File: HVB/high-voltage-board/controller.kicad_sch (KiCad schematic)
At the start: 25 parts, among them J10 Conn_01x05, U4 LD1117S33TR_SOT223, U5 STM32F413CGUx, U6 MCP2551-I-SN, Y1 Crystal

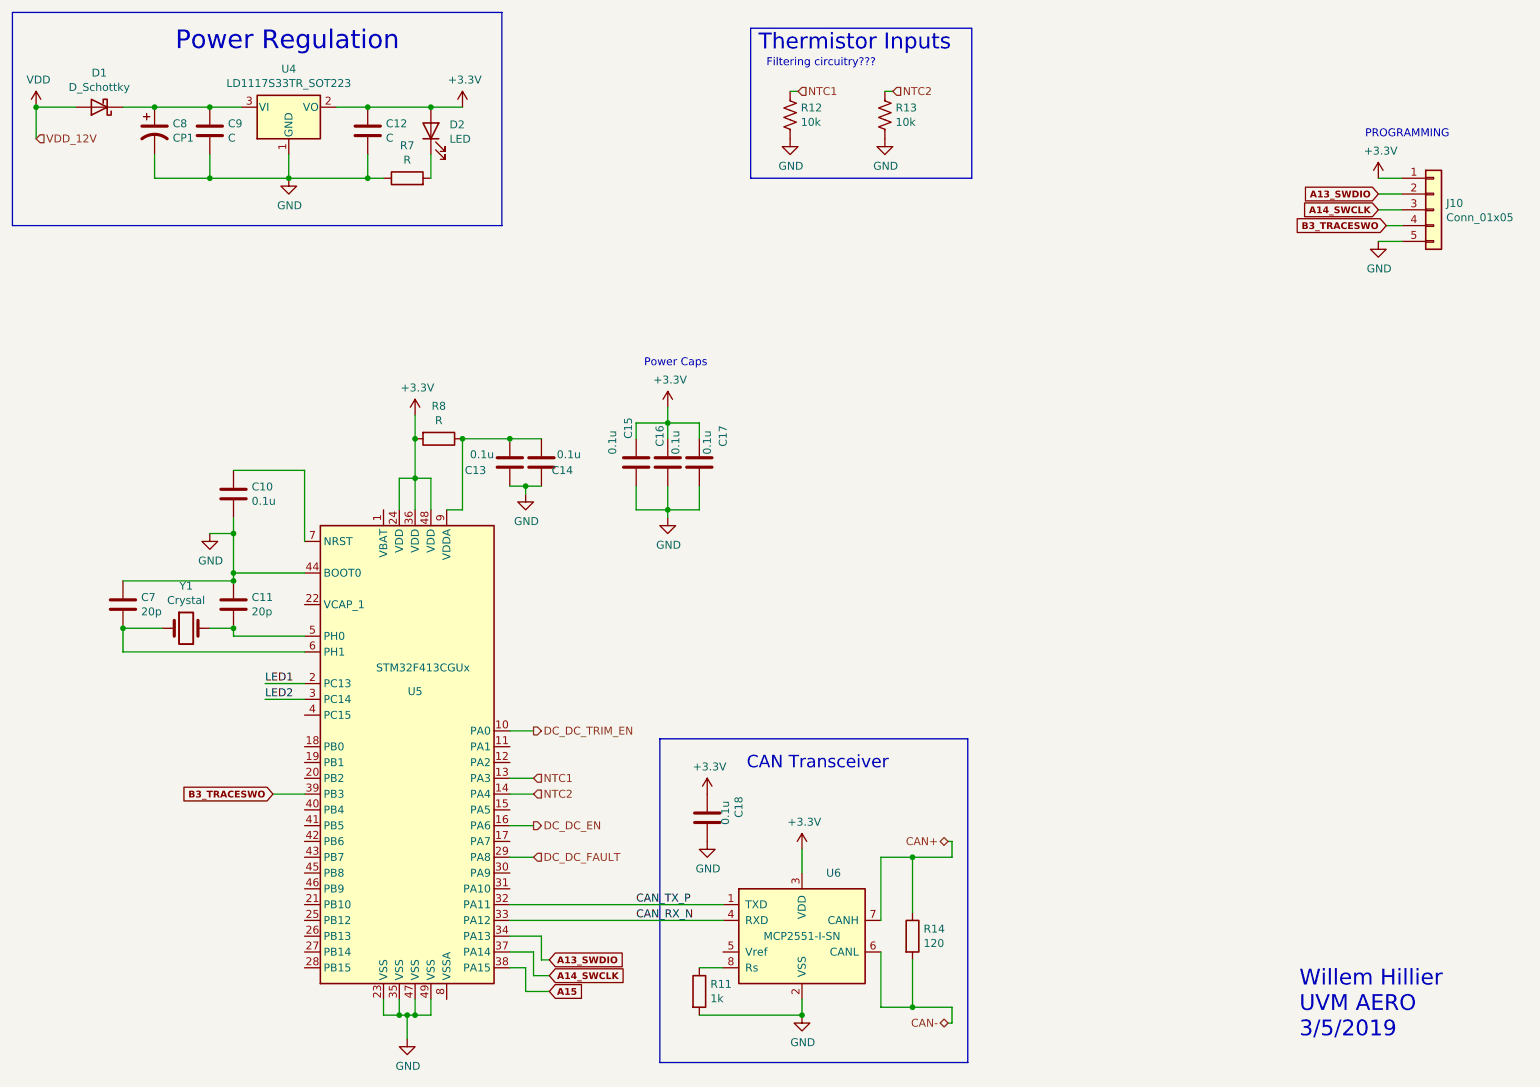
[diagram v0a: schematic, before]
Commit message: working on layout
Updating traces for RCB and organizing HVB
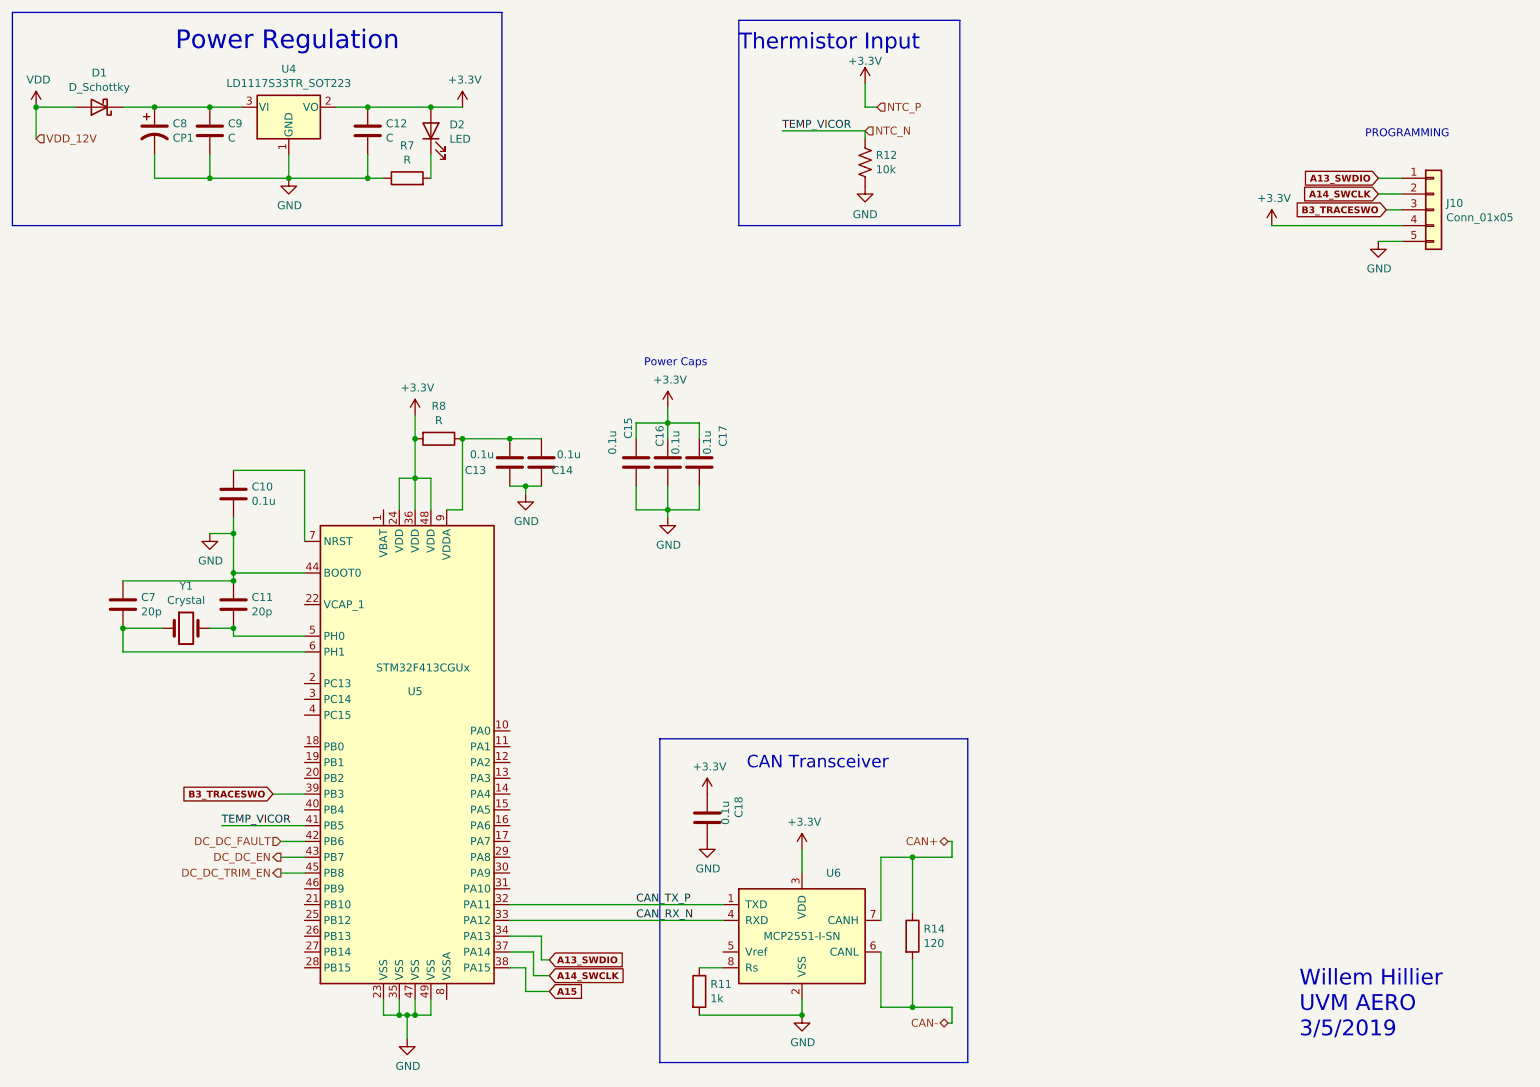
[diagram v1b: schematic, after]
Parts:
- removed R13: 10k, Resistor_SMD:R_0603_1608Metric_Pad0.98x0.95mm_HandSolder, symbol Device:R_US
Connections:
- net +3V3: now also J10.4 (Pin_4); no longer J10.1 (Pin_1)
- net A13_SWDIO: now also J10.1 (Pin_1); no longer J10.2 (Pin_2)
- net A14_SWCLK: now also J10.2 (Pin_2); no longer J10.3 (Pin_3)
- net B3_TRACESWO: now also J10.3 (Pin_3); no longer J10.4 (Pin_4)
- net DC_DC_EN: now also U5.43 (PB7); no longer U5.16 (PA6)
- net DC_DC_FAULT: now also U5.42 (PB6); no longer U5.29 (PA8)
- net DC_DC_TRIM_EN: now also U5.45 (PB8); no longer U5.10 (PA0)
- net NTC_N: now reaches U5.41 (PB5)
- net NTC_N: now also R12.2
- net LED1: no longer names the net of U5.2 (PC13)
- net LED2: no longer names the net of U5.3 (PC14)
- net NTC1: no longer names the net of U5.13 (PA3)
- net NTC1: no longer R12.2
- net NTC2: no longer names the net of U5.14 (PA4)
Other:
- note added: "Thermistor Input"
- note removed: "Filtering circuitry???"
- note removed: "Thermistor Inputs"
- moved on the sheet: R12

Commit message: updating hv layout
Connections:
- net VDD renamed +12V
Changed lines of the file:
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@@
   (junction (at 53.34 113.03) (diameter 0) (color 0 0 0 0)
   )
-  (junction (at 21.59 29.21) (diameter 0) (color 0 0 0 0)
-  )
   (junction (at 49.53 29.21) (diameter 0) (color 0 0 0 0)
   )
@@
   )
   (wire (pts (xy 85.09 40.64) (xy 85.09 36.83))
-    (stroke (width 0) (type default) (color 0 0 0 0))
-  )
-  (wire (pts (xy 21.59 34.29) (xy 21.59 29.21))
     (stroke (width 0) (type default) (color 0 0 0 0))
   )
@@
   (hierarchical_label "DC_DC_FAULT" (shape input) (at 60.96 147.32 180)
     (effects (font (size 1.27 1.27)) (justify right))
-  )
-  (hierarchical_label "VDD_12V" (shape input) (at 21.59 34.29 0)
-    (effects (font (size 1.27 1.27)) (justify left))
   )
   (hierarchical_label "DC_DC_EN" (shape output) (at 60.96 149.86 180)
@@
     (pin "1")
   )
-  (symbol (lib_id "power:VDD") (at 21.59 29.21 0) (unit 1)
-    (in_bom yes) (on_board yes)
-    (property "Reference" "#PWR024" (id 0) (at 21.59 33.02 0)
-      (effects (font (size 1.27 1.27)) hide)
-    )
-    (property "Value" "VDD" (id 1) (at 21.971 24.8158 0))
-    (property "Footprint" "" (id 2) (at 21.59 29.21 0)
-      (effects (font (size 1.27 1.27)) hide)
-    )
-    (property "Datasheet" "" (id 3) (at 21.59 29.21 0)
-      (effects (font (size 1.27 1.27)) hide)
-    )
-    (pin "1")
-  )
   (symbol (lib_id "Connector_Generic:Conn_01x05") (at 246.38 45.72 0) (unit 1)
     (in_bom yes) (on_board yes)
@@
       (effects (font (size 1.27 1.27)) hide)
     )
+    (pin "1")
+  )
+  (symbol (lib_id "power:+12V") (at 21.59 29.21 0) (unit 1)
+    (in_bom yes) (on_board yes) (fields_autoplaced)
+    (property "Reference" "#PWR0106" (id 0) (at 21.59 33.02 0)
+      (effects (font (size 1.27 1.27)) hide)
+    )
+    (property "Value" "+12V" (id 1) (at 21.59 25.6055 0))
+    (property "Footprint" "" (id 2) (at 21.59 29.21 0)
+      (effects (font (size 1.27 1.27)) hide)
+    )
+    (property "Datasheet" "" (id 3) (at 21.59 29.21 0)
+      (effects (font (size 1.27 1.27)) hide)
+    )

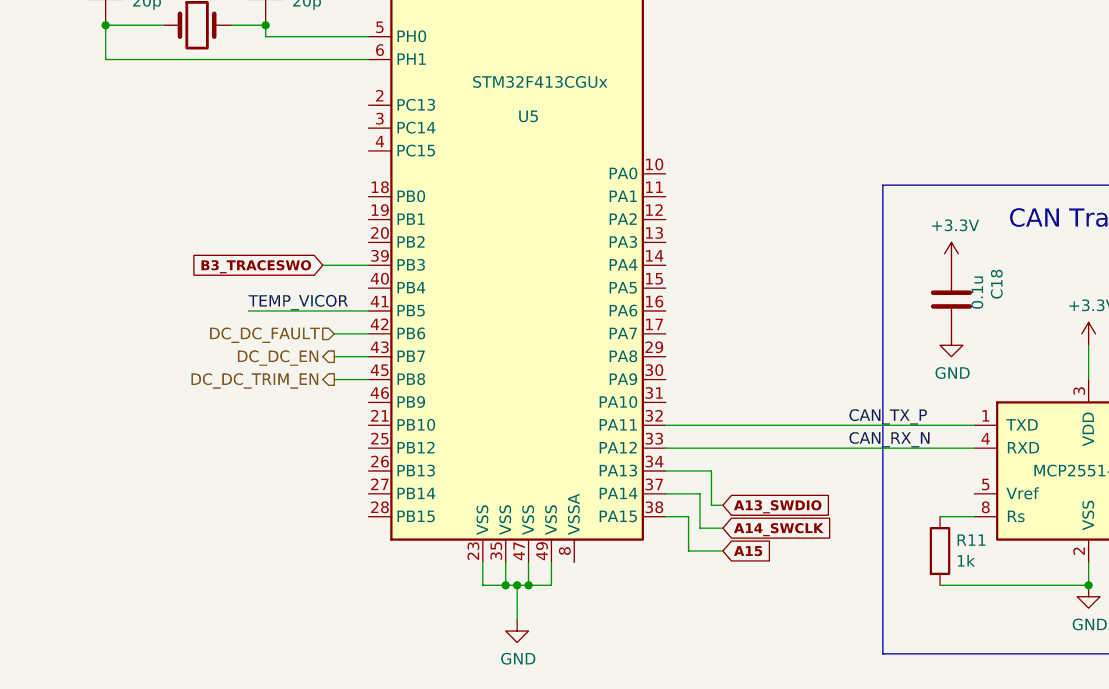
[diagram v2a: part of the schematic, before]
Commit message: almost done with layout
HV layout almost done. Tracing
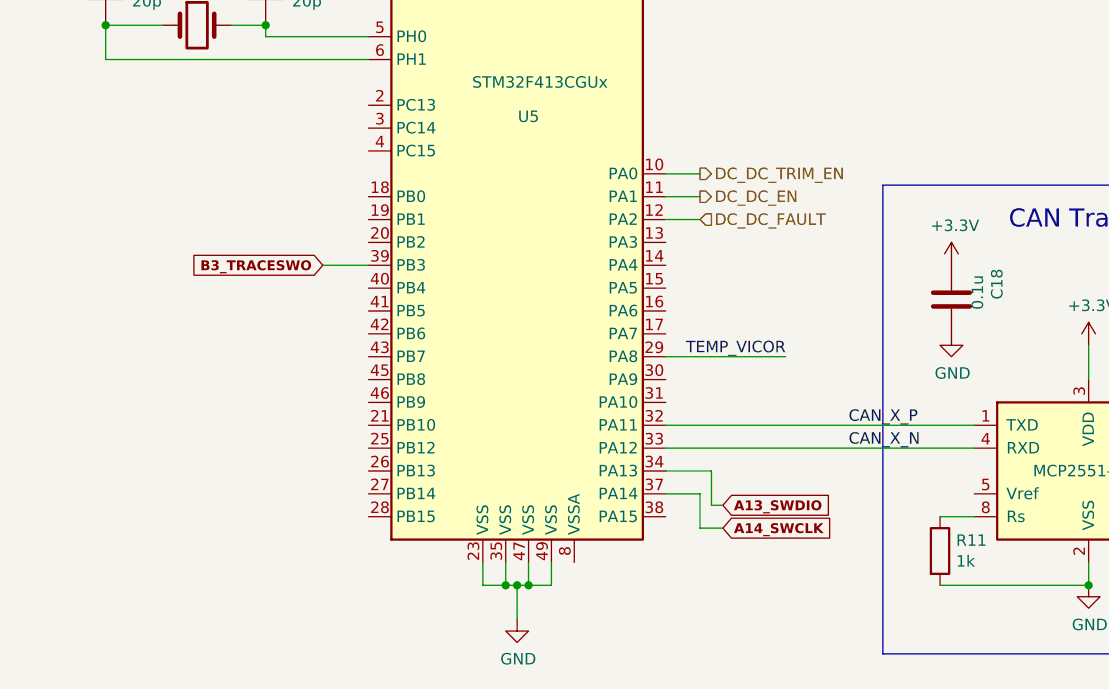
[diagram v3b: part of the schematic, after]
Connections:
- net DC_DC_EN: now also U5.11 (PA1); no longer U5.43 (PB7)
- net DC_DC_FAULT: now also U5.12 (PA2); no longer U5.42 (PB6)
- net DC_DC_TRIM_EN: now also U5.10 (PA0); no longer U5.45 (PB8)
- net NTC_N: now also U5.29 (PA8); no longer U5.41 (PB5)
- net A15: no longer names the net of U5.38 (PA15)
- net CAN_RX_N renamed CAN_X_N
- net CAN_TX_P renamed CAN_X_P
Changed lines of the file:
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@@
-    (stroke (width 0) (type default) (color 0 0 0 0))
-  )
-  (wire (pts (xy 100.33 171.45) (xy 104.14 171.45))
     (stroke (width 0) (type default) (color 0 0 0 0))
   )
@@
     (stroke (width 0) (type default) (color 0 0 0 0))
   )
-  (wire (pts (xy 60.96 149.86) (xy 64.77 149.86))
+  (wire (pts (xy 101.6 132.08) (xy 97.79 132.08))
     (stroke (width 0) (type default) (color 0 0 0 0))
   )
@@
     (stroke (width 0) (type default) (color 0 0 0 0))
   )
-  (wire (pts (xy 64.77 144.78) (xy 51.435 144.78))
+  (wire (pts (xy 97.79 149.86) (xy 111.125 149.86))
     (stroke (width 0) (type default) (color 0 0 0 0))
   )
@@
     (stroke (width 0) (type default) (color 0 0 0 0))
   )
-  (wire (pts (xy 97.79 167.64) (xy 100.33 167.64))
-    (stroke (width 0) (type default) (color 0 0 0 0))
-  )
   (wire (pts (xy 80.01 172.72) (xy 80.01 175.26))
     (stroke (width 0) (type default) (color 0 0 0 0))
@@
     (stroke (width 0) (type default) (color 0 0 0 0))
   )
-  (wire (pts (xy 100.33 167.64) (xy 100.33 171.45))
-    (stroke (width 0) (type default) (color 0 0 0 0))
-  )
   (wire (pts (xy 154.94 34.29) (xy 154.94 33.02))
     (stroke (width 0) (type default) (color 0 0 0 0))
   )
-  (wire (pts (xy 60.96 147.32) (xy 64.77 147.32))
+  (wire (pts (xy 101.6 134.62) (xy 97.79 134.62))
     (stroke (width 0) (type default) (color 0 0 0 0))
   )
@@
     (stroke (width 0) (type default) (color 0 0 0 0))
   )
-  (wire (pts (xy 60.96 152.4) (xy 64.77 152.4))
+  (wire (pts (xy 101.6 129.54) (xy 97.79 129.54))
     (stroke (width 0) (type default) (color 0 0 0 0))
   )
@@
     (effects (font (size 2.9972 2.9972)) (justify right bottom))
   )
-  (label "CAN_RX_N" (at 118.11 160.02 0)
+  (label "CAN_X_N" (at 118.11 160.02 0)
     (effects (font (size 1.27 1.27)) (justify left bottom))
   )
-  (label "CAN_TX_P" (at 118.11 157.48 0)
+  (label "CAN_X_P" (at 118.11 157.48 0)
     (effects (font (size 1.27 1.27)) (justify left bottom))
   )
-  (label "TEMP_VICOR" (at 51.435 144.78 0)
-    (effects (font (size 1.27 1.27)) (justify left bottom))
+  (label "TEMP_VICOR" (at 111.125 149.86 180)
+    (effects (font (size 1.27 1.27)) (justify right bottom))
   )
   (label "TEMP_VICOR" (at 141.605 33.02 0)
@@
     )
   )
-  (global_label "A15" (shape input) (at 104.14 171.45 0) (fields_autoplaced)
-    (effects (font (size 1.0922 1.0922) (thickness 0.2184) bold) (justify left))
-    (property "Intersheet References" "${INTERSHEET_REFS}" (id 0) (at 0 0 0)
-      (effects (font (size 1.27 1.27)) hide)
-    )
-  )
   (global_label "A14_SWCLK" (shape input) (at 104.14 168.91 0) (fields_autoplaced)
     (effects (font (size 1.0922 1.0922) (thickness 0.2184) bold) (justify left))
@@
     (effects (font (size 1.27 1.27)) (justify right))
   )
-  (hierarchical_label "DC_DC_FAULT" (shape input) (at 60.96 147.32 180)
-    (effects (font (size 1.27 1.27)) (justify right))
-  )
-  (hierarchical_label "DC_DC_EN" (shape output) (at 60.96 149.86 180)
-    (effects (font (size 1.27 1.27)) (justify right))
+  (hierarchical_label "DC_DC_FAULT" (shape input) (at 101.6 134.62 0)
+    (effects (font (size 1.27 1.27)) (justify left))
+  )
+  (hierarchical_label "DC_DC_EN" (shape output) (at 101.6 132.08 0)
+    (effects (font (size 1.27 1.27)) (justify left))
   )
   (hierarchical_label "CAN+" (shape bidirectional) (at 168.275 147.32 180)
     (effects (font (size 1.27 1.27)) (justify right))
   )
-  (hierarchical_label "DC_DC_TRIM_EN" (shape output) (at 60.96 152.4 180)
-    (effects (font (size 1.27 1.27)) (justify right))
+  (hierarchical_label "DC_DC_TRIM_EN" (shape output) (at 101.6 129.54 0)
+    (effects (font (size 1.27 1.27)) (justify left))
   )
   (symbol (lib_id "Device:R_US") (at 154.94 38.1 180) (unit 1)

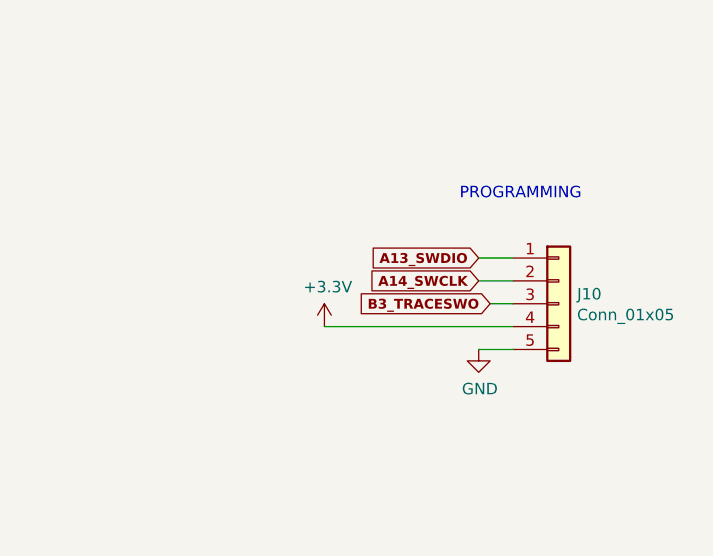
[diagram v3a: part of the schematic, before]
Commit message: updating pcb size and layout
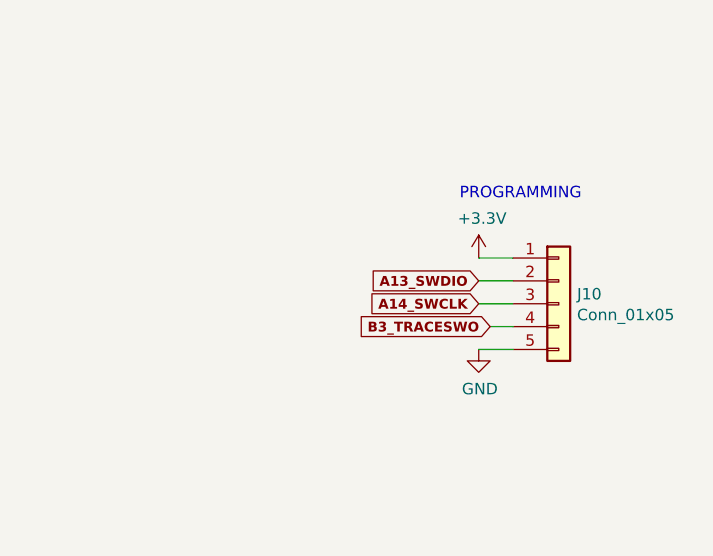
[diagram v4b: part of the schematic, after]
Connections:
- net +3V3: now also J10.1 (Pin_1); no longer J10.4 (Pin_4)
- net A13_SWDIO: now also J10.2 (Pin_2); no longer J10.1 (Pin_1)
- net A14_SWCLK: now also J10.3 (Pin_3); no longer J10.2 (Pin_2)
- net B3_TRACESWO: now also J10.4 (Pin_4); no longer J10.3 (Pin_3)

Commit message: Layout Trace Complete
completed layout of tracks. Still need to place silkscreens
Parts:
- U5: footprint Package_DFN_QFN:QFN-48-1EP_7x7mm_P0.5mm_EP5.3x5.3mm_ThermalVias -> Package_DFN_QFN:QFN-48-1EP_7x7mm_P0.5mm_EP5.3x5.3mm
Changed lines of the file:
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@@
     (property "Reference" "U5" (id 0) (at 82.55 123.19 0))
     (property "Value" "STM32F413CGUx" (id 1) (at 83.82 119.38 0))
-    (property "Footprint" "Package_DFN_QFN:QFN-48-1EP_7x7mm_P0.5mm_EP5.3x5.3mm_ThermalVias" (id 2) (at 67.31 170.18 0)
+    (property "Footprint" "Package_DFN_QFN:QFN-48-1EP_7x7mm_P0.5mm_EP5.3x5.3mm" (id 2) (at 67.31 170.18 0)
       (effects (font (size 1.27 1.27)) (justify right) hide)
     )

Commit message: updating pinout
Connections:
- net NTC_N: now also U5.17 (PA7); no longer U5.29 (PA8)
- net DC_DC_TRIM_EN: no longer names the net of U5.10 (PA0)
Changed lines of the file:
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@@
     (stroke (width 0) (type default) (color 0 0 0 0))
   )
-  (wire (pts (xy 97.79 149.86) (xy 111.125 149.86))
+  (wire (pts (xy 97.79 147.32) (xy 111.125 147.32))
     (stroke (width 0) (type default) (color 0 0 0 0))
   )
@@
     (stroke (width 0) (type default) (color 0 0 0 0))
   )
-  (wire (pts (xy 101.6 129.54) (xy 97.79 129.54))
-    (stroke (width 0) (type default) (color 0 0 0 0))
-  )
   (wire (pts (xy 40.64 29.21) (xy 49.53 29.21))
     (stroke (width 0) (type default) (color 0 0 0 0))
@@
     (effects (font (size 1.27 1.27)) (justify left bottom))
   )
-  (label "TEMP_VICOR" (at 111.125 149.86 180)
+  (label "TEMP_VICOR" (at 111.125 147.32 180)
     (effects (font (size 1.27 1.27)) (justify right bottom))
   )
@@
     (effects (font (size 1.27 1.27)) (justify right))
   )
-  (hierarchical_label "DC_DC_TRIM_EN" (shape output) (at 101.6 129.54 0)
-    (effects (font (size 1.27 1.27)) (justify left))
-  )
   (symbol (lib_id "Device:R_US") (at 154.94 38.1 180) (unit 1)
